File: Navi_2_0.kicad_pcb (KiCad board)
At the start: 4 copper layers, 111.7 x 136.9 mm, 98 parts, among them J1 USB_B_Micro, J10 BAT-, J2 Conn_01x24_Male, J27 Micro_SD_Card_Det, J9 BAT+, Q1 DMG2301L-7, Q2 TF2310, Q3 DMG2301L-7, Q4 Q_NPN_BEC, Q5 Q_NPN_BEC, Q6 DMG2301L-7, Q7 DMG2301L-7, SW1 SW_Push, SW2 SW_Push, U1 MT3420C, U2 MT3420C, U3 ESP32-WROOM-32, U4 CH340K, U5 L96-M33, U6 LSM303AH, U7 TCN75-3.3

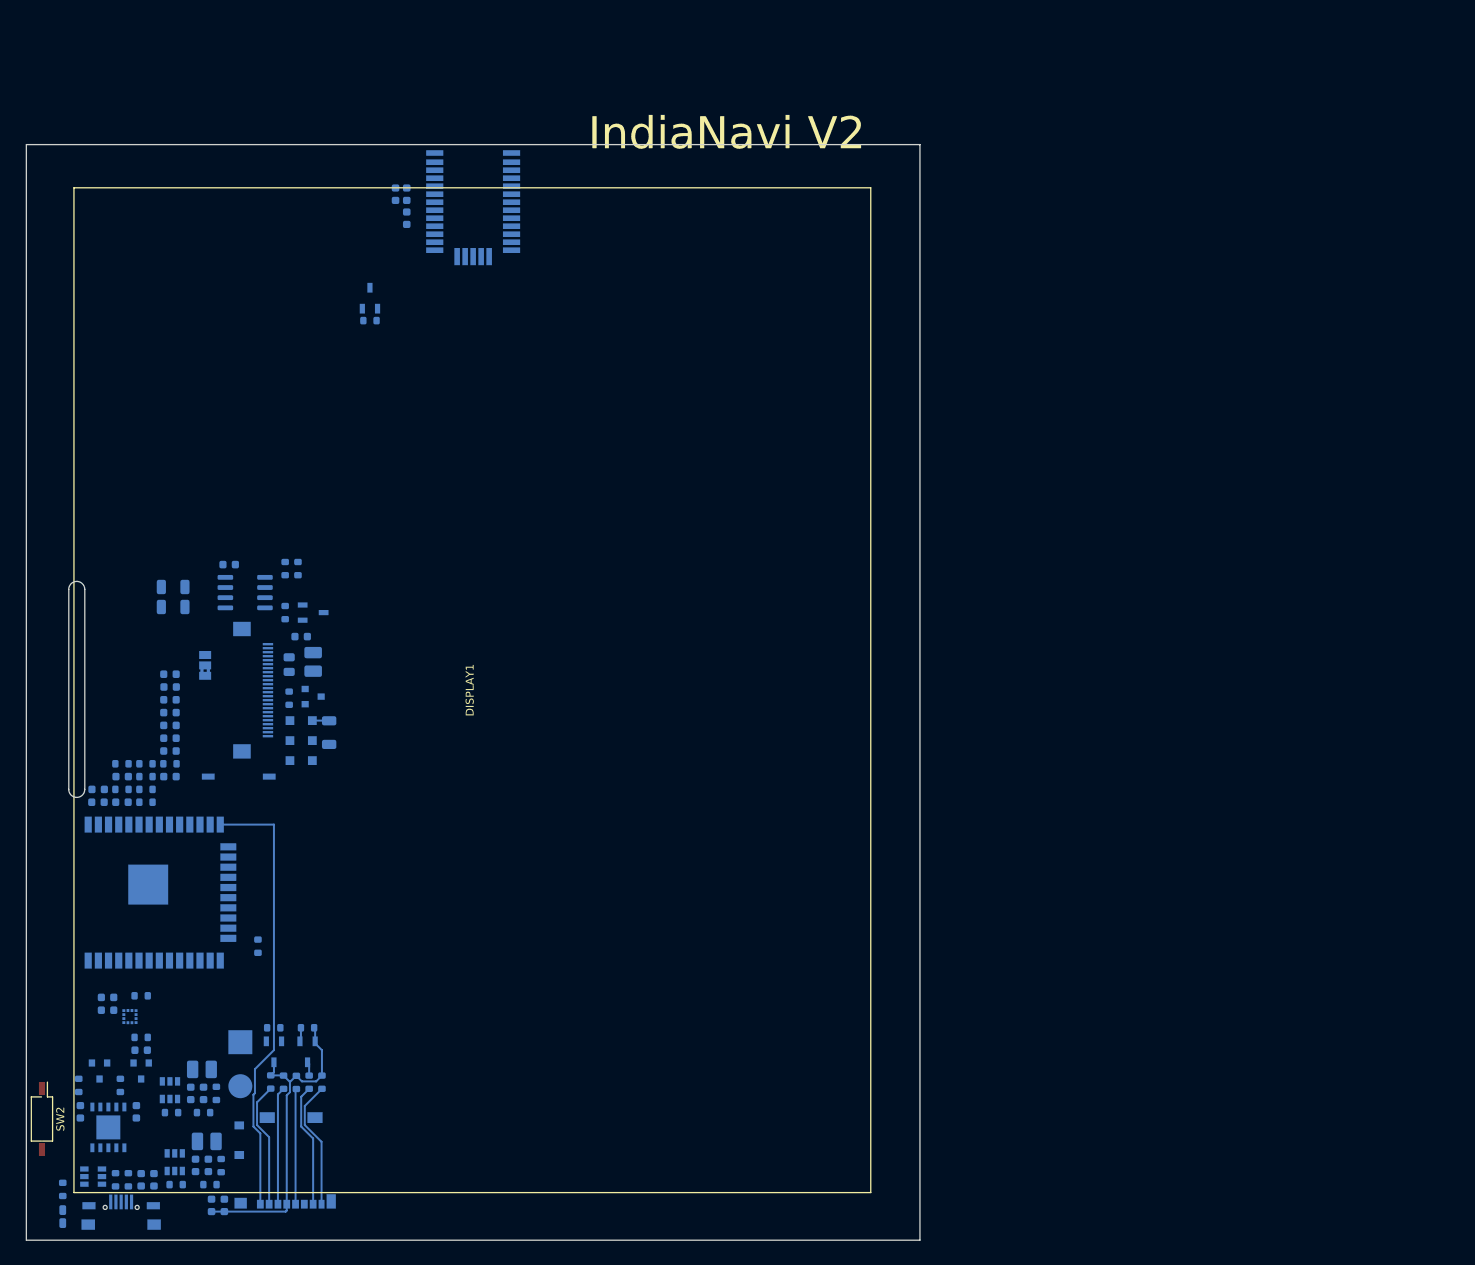
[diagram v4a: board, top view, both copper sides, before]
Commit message: Layout V3 erster Wurf
Layout V3 vor DRC
(Siebdruck und Leiterbahnen fertig)
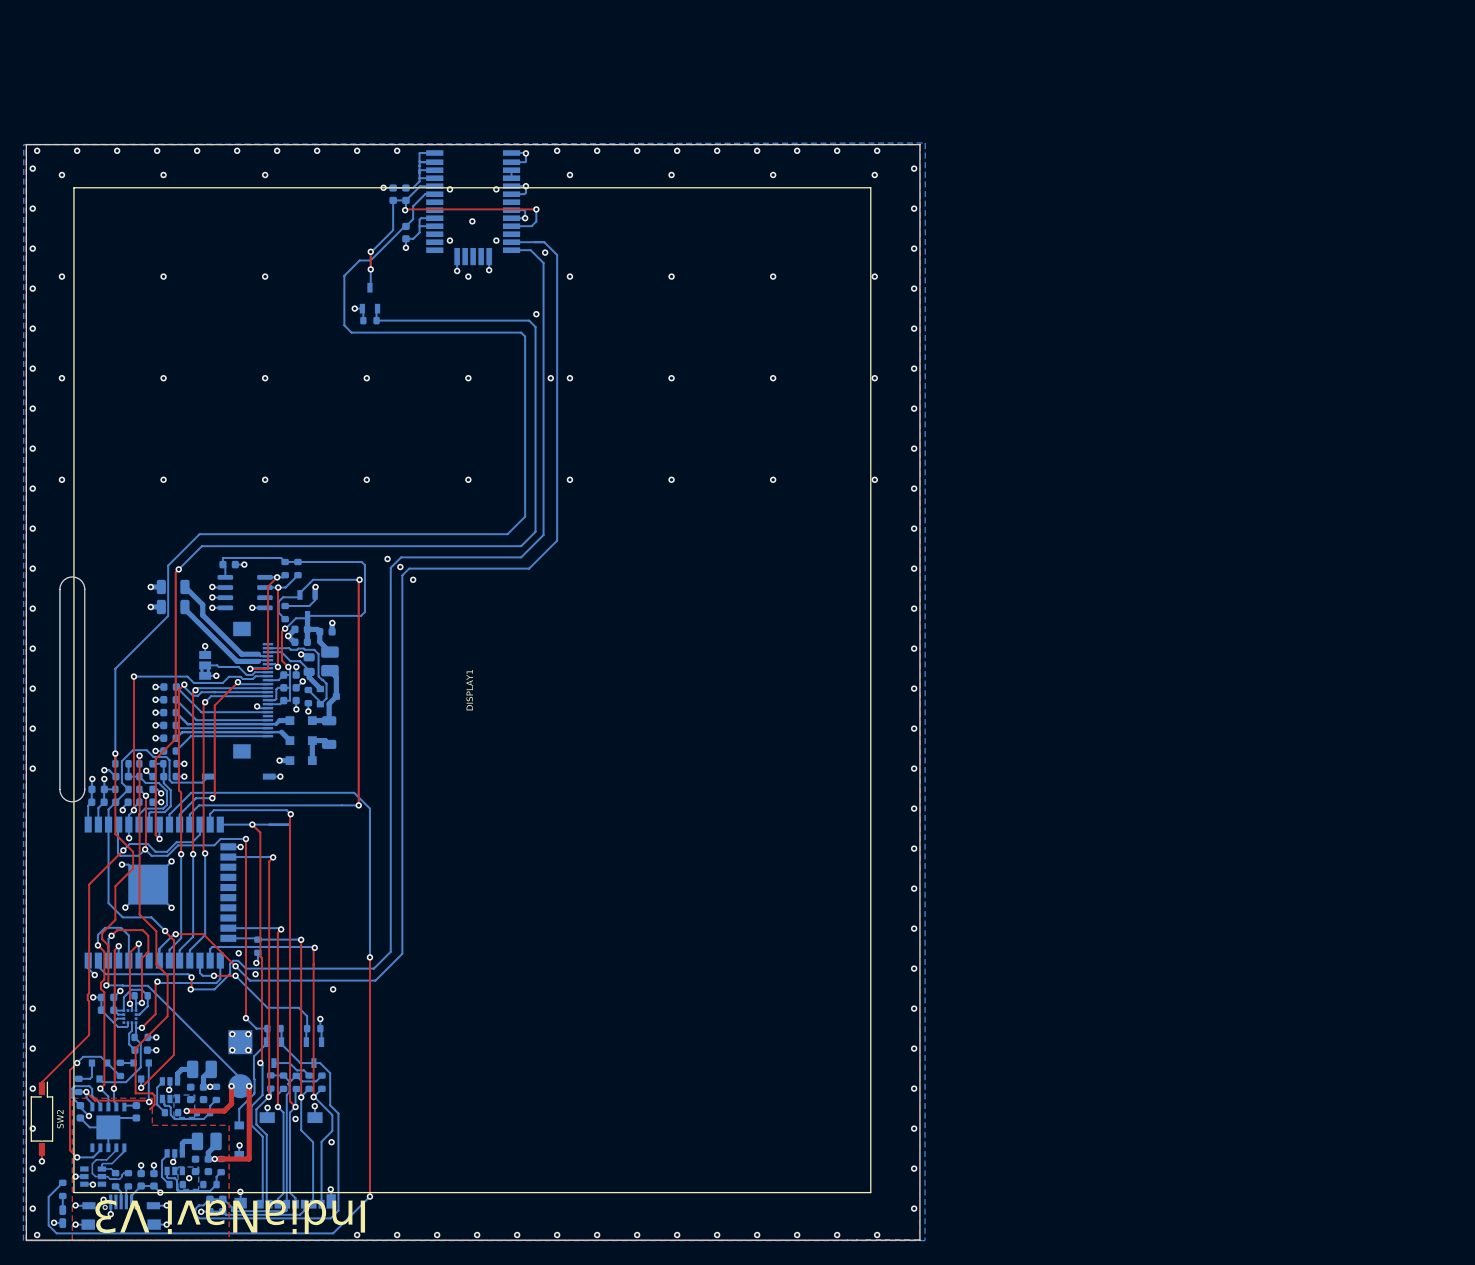
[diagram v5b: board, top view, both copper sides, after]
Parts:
- added C34: 220n, Capacitor_SMD:C_0603_1608Metric, B.Cu at (66.6, 113.3)
- added C35: 220n, Capacitor_SMD:C_0603_1608Metric, B.Cu at (66.6, 114.9)
- added C36: 4µ7, Capacitor_SMD:C_0603_1608Metric, B.Cu at (71.1, 107.9)
- added C37: 4µ7, Capacitor_SMD:C_0603_1608Metric, B.Cu at (68.0, 109.2)
- moved C26 15.4 mm to (66.6, 116.5), turned to 0 degrees
- moved Q6 5.00 mm to (69.6, 160.5)
- moved R33 5.00 mm to (69.6, 157.5)
- moved Q7 4.20 mm to (64.6, 160.5)
- moved R23 4.20 mm to (64.6, 157.5)
- moved R28 2.50 mm to (69.0, 112.0)
- moved R29 2.41 mm to (68.9, 116.0)
- moved L3 2.10 mm to (71.6, 111.6)
- moved R19 2.00 mm to (45.4, 162.6)
- moved Q2 1.90 mm to (71.4, 116.0)
- moved C31 1.80 mm to (81.1, 58.0), turned to -90 degrees
- moved C18 1.80 mm to (56.6, 179.6), turned to -90 degrees
- moved C22 1.60 mm to (51.6, 121.2)
- moved C29 1.60 mm to (51.6, 119.6)
- moved C19 1.40 mm to (58.2, 179.6), turned to 90 degrees
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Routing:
- net +BATT: track 0.00 -> 223.5 mm, vias 0 -> 6
- net GND: track 0.00 -> 167.4 mm, vias 0 -> 201
- net UART_GPS_TX: track 0.00 -> 150.5 mm, vias 0 -> 2
- net UART_GPS_RX: track 0.00 -> 148.4 mm, vias 0 -> 2
- net GPS_VCC_nEN: track 0.00 -> 130.8 mm, vias 0 -> 2
- net Net-(R18-Pad2): track 0.00 -> 125.3 mm, vias 0 -> 2
- net +5V: track 0.00 -> 66.8 mm, vias 0 -> 5
- net SD_nDET: track 1.74 -> 68.4 mm, vias 0 -> 4
- net EINK_VCC: track 0.00 -> 65.7 mm, vias 0 -> 2
- net ESP_~RST: track 0.00 -> 65.3 mm, vias 0 -> 2
- net EINK_VCC_~EN: track 0.00 -> 64.9 mm, vias 0 -> 2
- net SD_CLK: track 14.4 -> 63.8 mm, vias 0 -> 2
- net EINK_SPI_CLK: track 0.00 -> 47.1 mm, vias 0 -> 2
- net Net-(SW2-Pad1): track 0.00 -> 46.6 mm, vias 0 -> 1
- net EINK_~CS: track 0.00 -> 43.8 mm, vias 0 -> 2
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- added copper zone on F.Cu, net +3V3
- added copper zone on B.Cu, net +5V
- added copper zone on F.Cu, net +5V
- added copper zone on B.Cu, net +BATT
- added copper zone on B.Cu, net GND
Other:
- outline, holes or cut-outs redrawn
- board text added: "IndiaNavi V3"
- board text removed: "IndiaNavi V2"

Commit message: changing inductor and connecting reset
Changed Indoctor 4,7µ to 10µ
Connected reset button to 3V3 supply enamble regulator #11
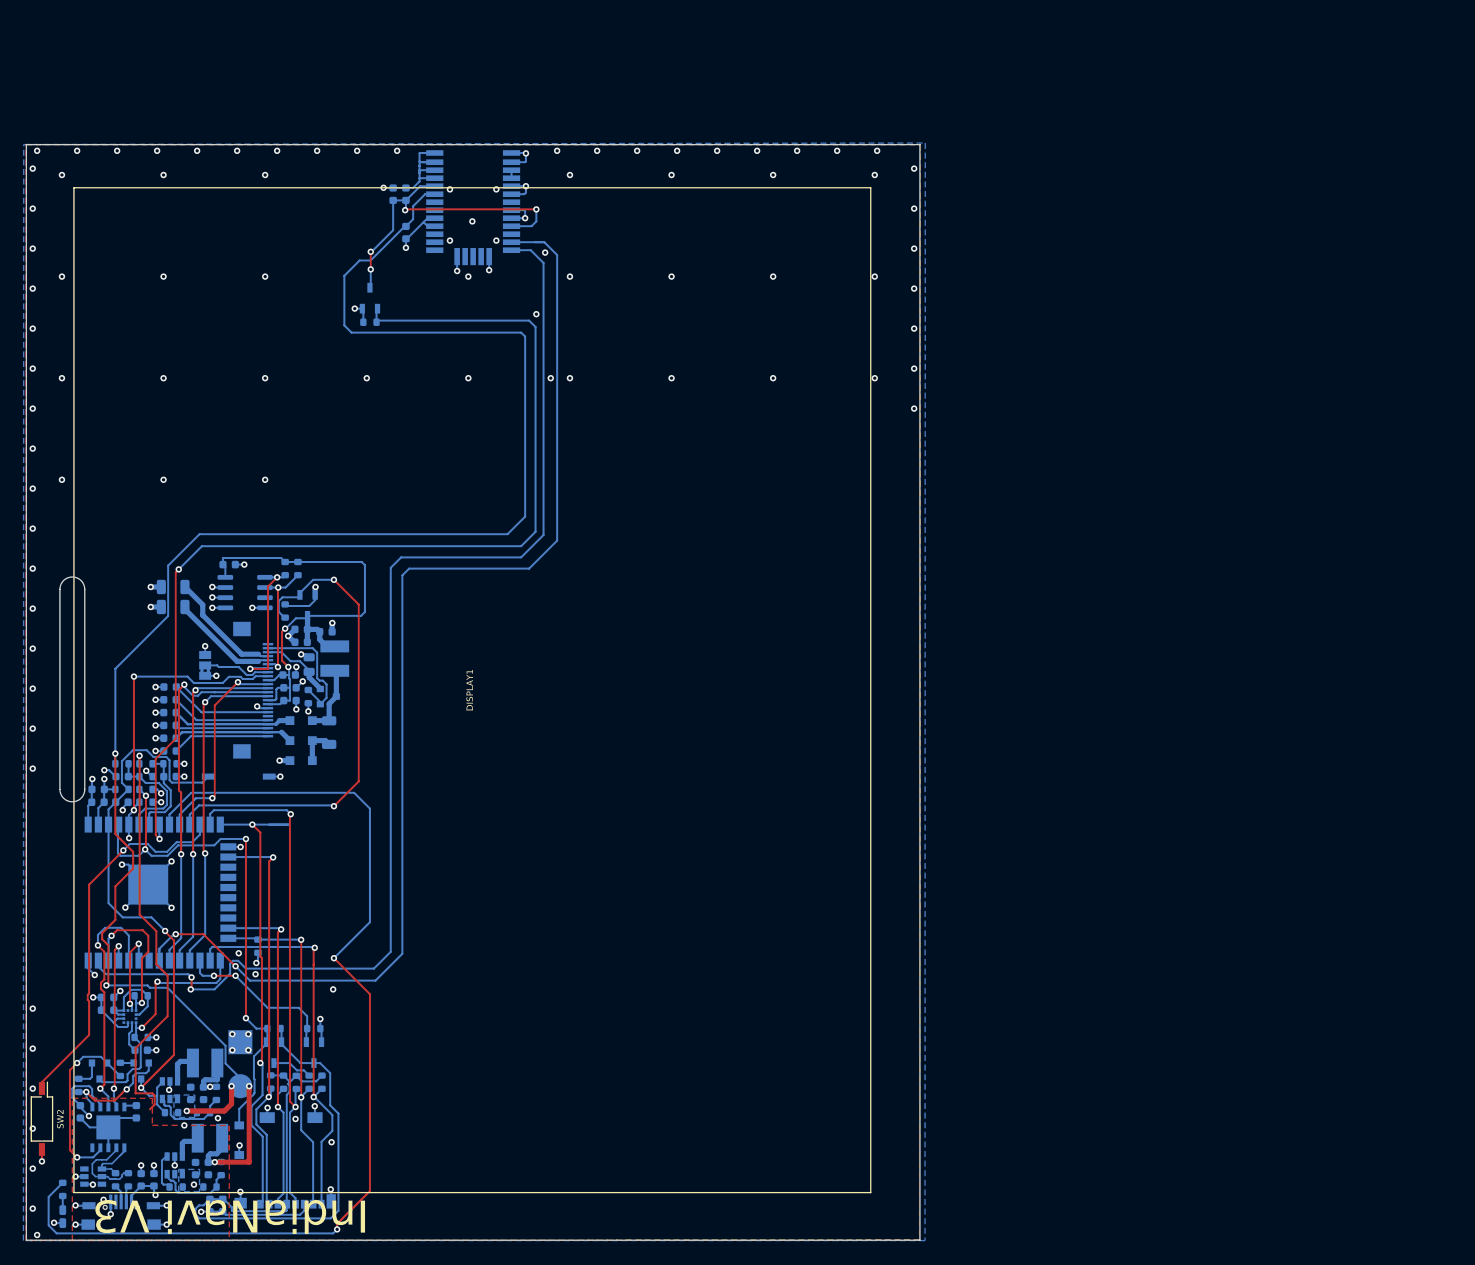
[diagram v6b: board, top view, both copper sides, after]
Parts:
- L1, L2, L3: value 4µ7 -> 10µ; footprint Inductor_SMD:L_1008_2520Metric_Pad1.43x2.20mm_HandSolder -> Inductor_SMD:L_Bourns-SRN4018
- moved L2 0.89 mm to (56.0, 161.8)
- moved L3 0.69 mm to (72.2, 111.2)
- moved L1 0.57 mm to (56.6, 171.2)
- moved C1 0.40 mm to (54.8, 175.0)
- moved C10 0.40 mm to (56.4, 175.0)
- moved U1 0.40 mm to (52.2, 174.6)
- moved R10 0.38 mm to (58.0, 175.0)
- moved R11 0.30 mm to (56.6, 177.3)
- moved R2 0.30 mm to (52.4, 177.3)
- moved R27 0.20 mm to (66.0, 105.3)
- moved R32 0.20 mm to (76.6, 69.2)
- moved C34 0.10 mm to (66.5, 113.3)
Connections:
- R3 pad 1: Net-(R3-Pad1) -> ESP_~RST
- U2 pad 1: Net-(R3-Pad1) -> ESP_~RST
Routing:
- net ESP_~RST: track 65.3 -> 72.3 mm
- net Net-(R3-Pad1): track 4.57 -> 0.00 mm
- net Net-(R18-Pad2): track 125.3 -> 129.0 mm
- net EINK_VCC_~EN: track 64.9 -> 61.3 mm
- net +BATT: track 223.5 -> 226.8 mm
- net Net-(Q4-Pad2): track 17.4 -> 15.3 mm
- net +3V3: track 41.4 -> 43.4 mm
- net Net-(L2-Pad1): track 3.07 -> 4.30 mm
- net GND: track 167.4 -> 166.5 mm, vias 201 -> 160

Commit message: Add Readme an PICs
Add Readme.md without text
Add PICs
Add 3D Models
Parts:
- added G***: LOGO, Navi_1_0-backups:Platinenmacher_14, B.Cu at (44.9, 69.9)
- added REF**: KiCad-Logo2_12mm_SilkScreen, Symbol:KiCad-Logo2_12mm_SilkScreen, B.Cu at (123.7, 59.8)
- added REF**: ESD-Logo_13.2x12mm_SilkScreen, Symbol:ESD-Logo_13.2x12mm_SilkScreen, B.Cu at (44.4, 58.1)
- added SM3: SYM_Arrow45_Tiny, TheBrutzlers_Lib:Symbol_kurzschlussblog, F.Cu at (139.4, 65.4)
- added SM3: SYM_Arrow45_Tiny, TheBrutzlers_Lib:Symbol_kurzschlussblog, B.Cu at (61.0, 71.0)
- added SM3: SYM_Arrow45_Tiny, TheBrutzlers_Lib:Symbol_kurzschlussblog, B.Cu at (61.0, 66.0)
- added SM3: SYM_Arrow45_Tiny, TheBrutzlers_Lib:Symbol_kurzschlussblog, B.Cu at (55.0, 66.0)
- added SM3: SYM_Arrow45_Tiny, TheBrutzlers_Lib:Symbol_kurzschlussblog, B.Cu at (55.0, 71.0)
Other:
- board text added: "BAT+"
- board text added: "BAT-"
- board text added: "IndiaNavi"
- board text added: "https://github.com/DasBasti/IndiaNavi_PCB"
- board text added: "theBrutzler Platinenmacher"
- board text added: "www.kurzschluss-junkies.de"
- board text removed: "IndiaNavi V3"

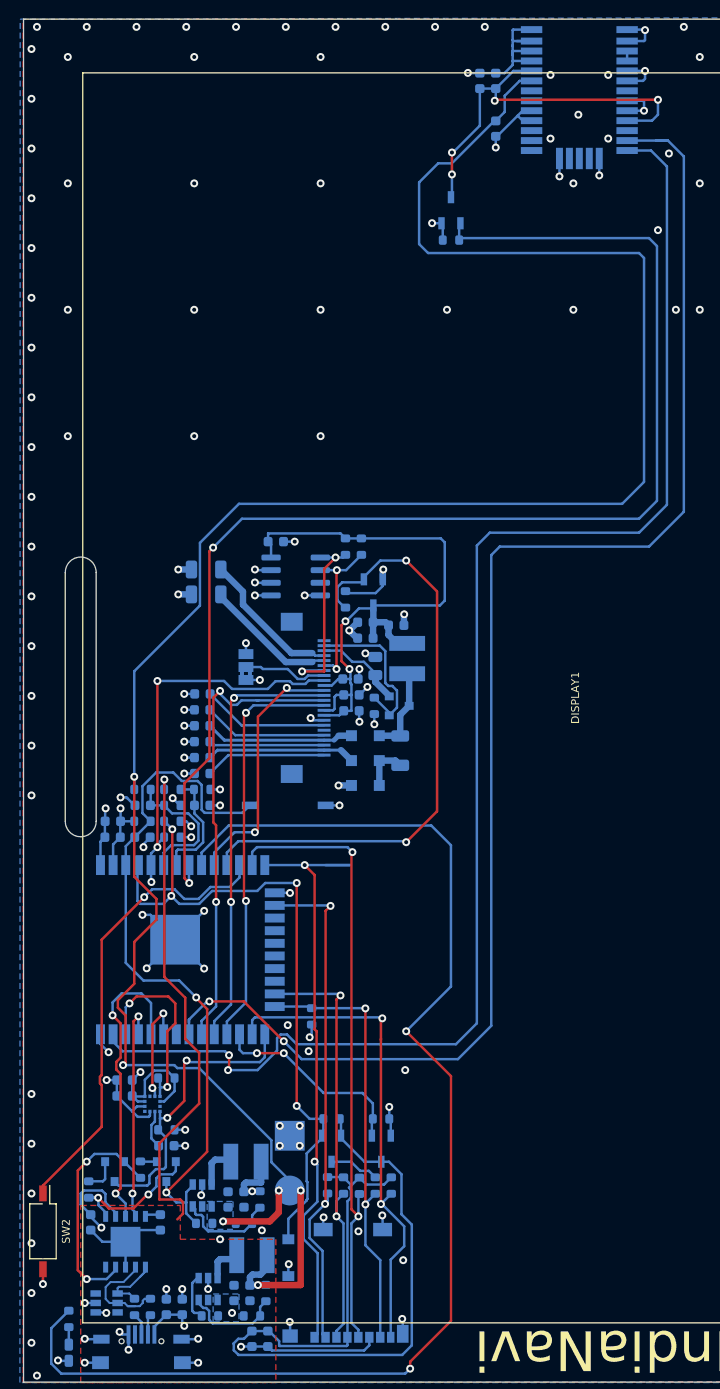
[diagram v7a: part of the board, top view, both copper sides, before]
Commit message: Ordered PCB
Final layout PCB after DRC check ordered.
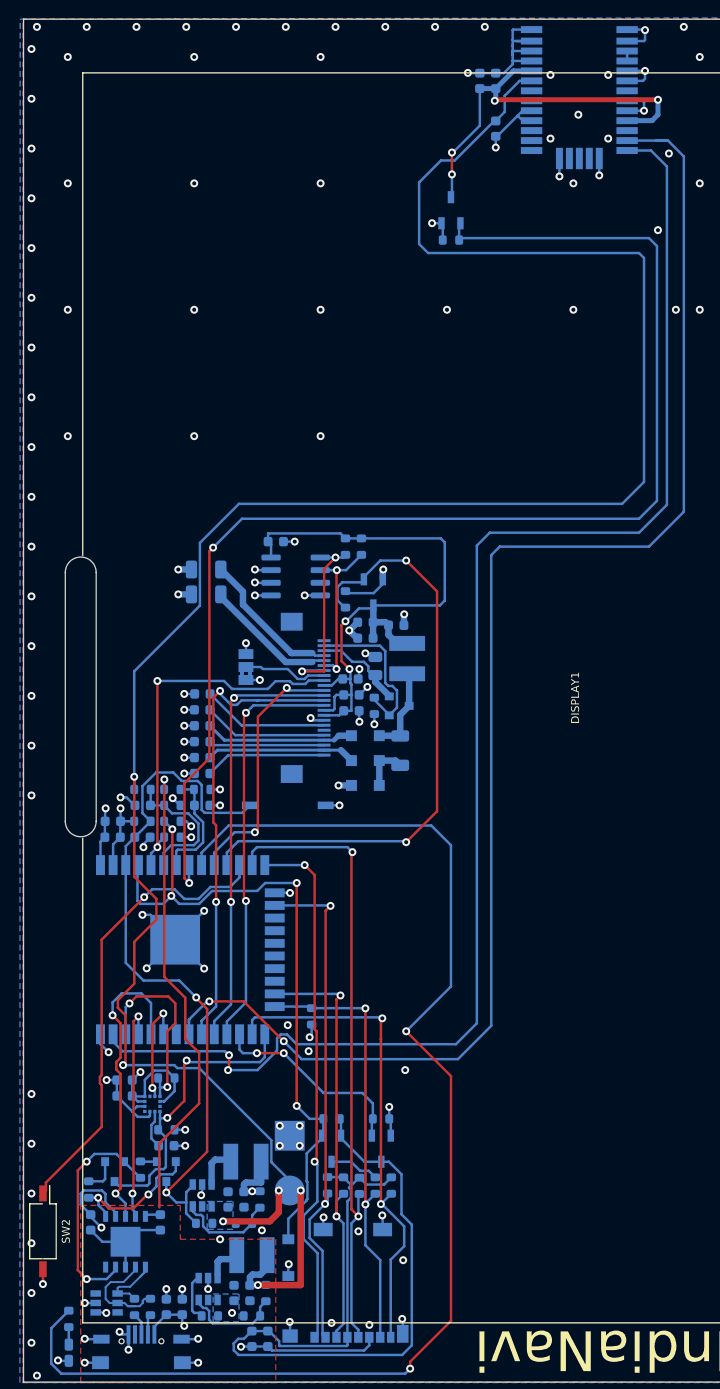
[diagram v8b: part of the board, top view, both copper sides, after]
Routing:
- net SD_DAT2: track 60.5 -> 53.4 mm
- net +5V: track 66.9 -> 63.2 mm
- net EINK_STATE: track 39.4 -> 37.7 mm, vias 3 -> 2
- net GND: vias 160 -> 162
